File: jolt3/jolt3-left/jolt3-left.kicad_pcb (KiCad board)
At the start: 2 copper layers, 151 x 98 mm, 33 parts, among them J1 Conn_01x02_Pin, J10 Conn_01x02_Pin, J11 Conn_01x02_Pin, J12 Conn_01x02_Pin, J13 Conn_01x02_Pin, J14 Conn_01x02_Pin, J15 Conn_01x02_Pin, J16 Conn_01x02_Pin, J17 Conn_01x02_Pin, J18 Conn_01x02_Pin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

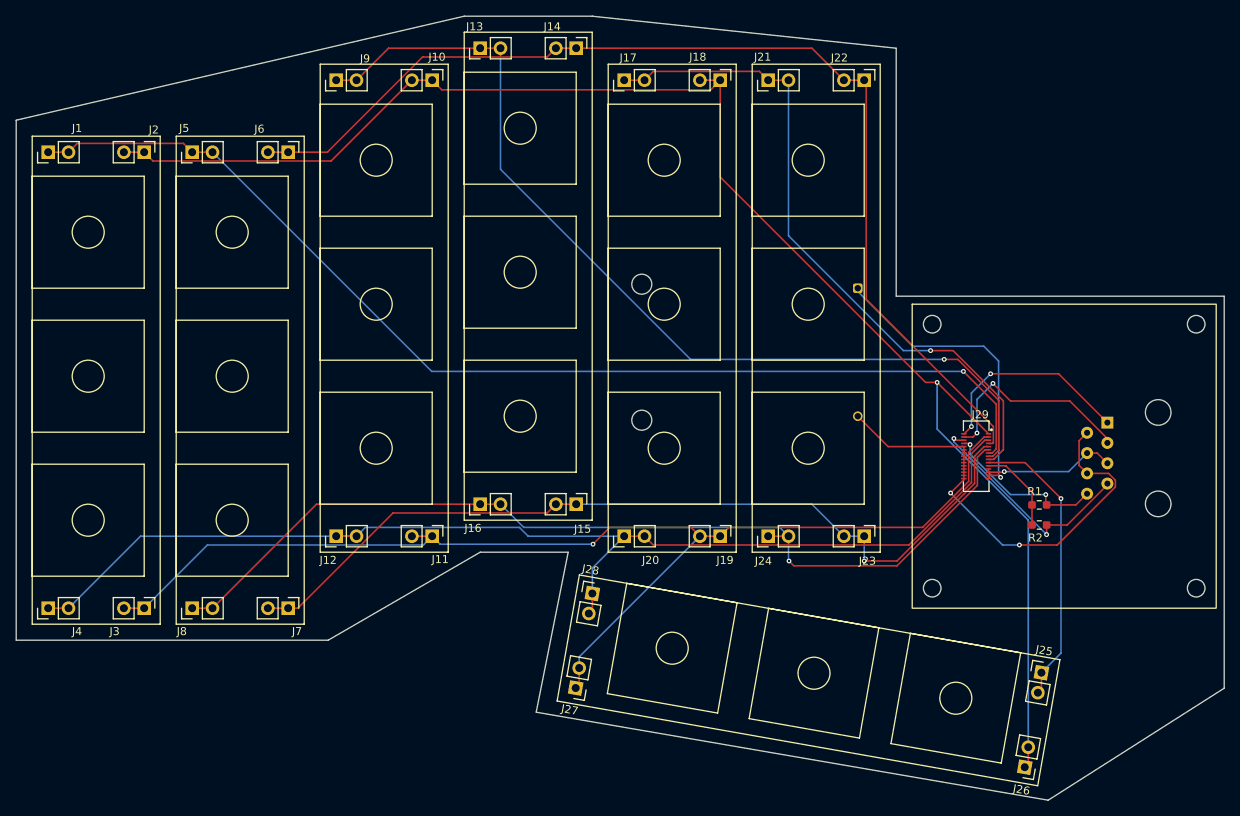
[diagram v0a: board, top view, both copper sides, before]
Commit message: Jolt 3: Rev A for 3 boards
Send Rev A out for jolt3-left, jolt3-right, and j3-mez-2040.
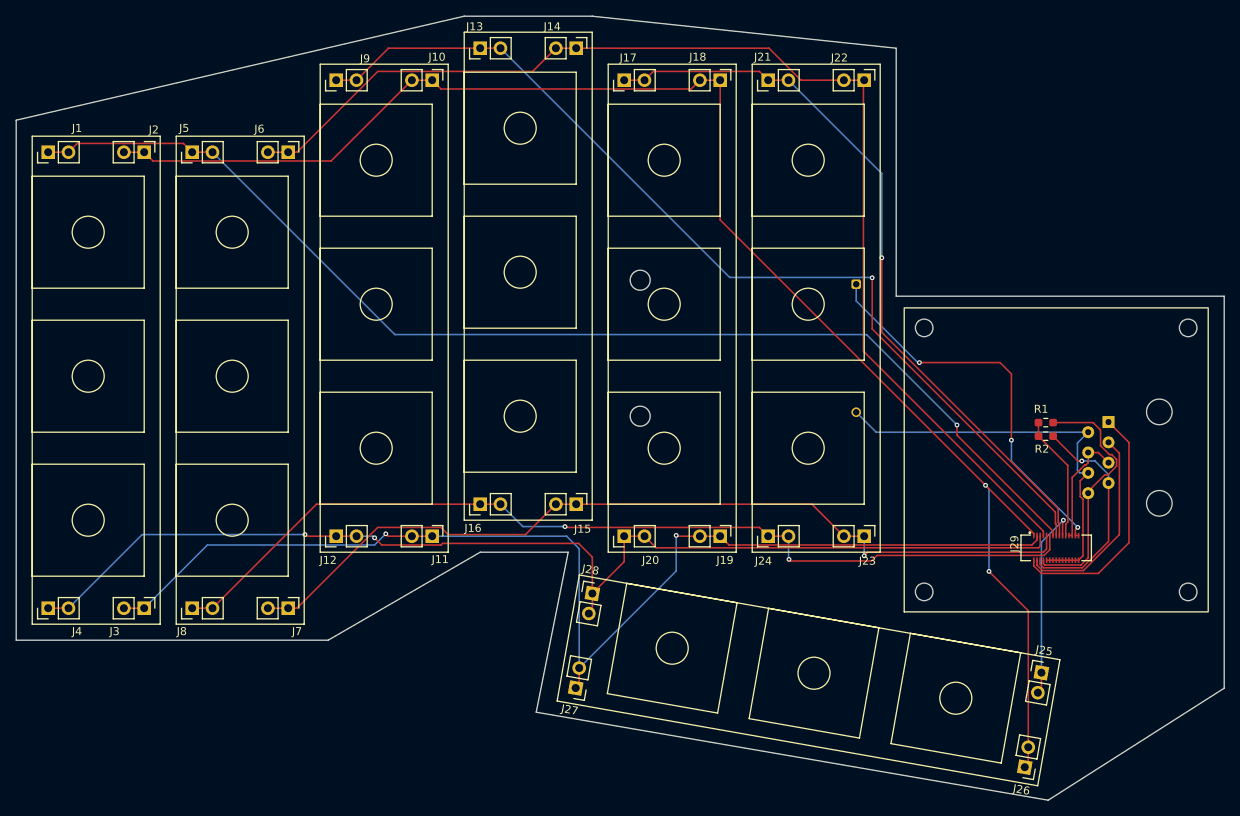
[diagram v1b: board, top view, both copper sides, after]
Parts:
- moved J29 15.2 mm to (167.0, 134.5), turned to 90 degrees
- moved R2 11.1 mm to (165.7, 120.5)
- moved R1 10.3 mm to (165.7, 118.8)
- moved BT1 0.54 mm to (144.0, 125.5)
- moved J31 0.16 mm to (173.5, 118.7)
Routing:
- net /ROW-D: track 134.2 -> 147.9 mm
- net /COL-D: track 36.4 -> 24.8 mm
- net Net-(BT1-+): track 38.5 -> 49.4 mm, vias 1 -> 3
- net /SDA: track 20.6 -> 31.4 mm, vias 2 -> 0
- net /COL-A: track 139.2 -> 147.4 mm
- net /COL-C: track 84.8 -> 92.4 mm
- net GND: track 58.3 -> 52.6 mm, vias 2 -> 0
- net +3.3V: track 10.9 -> 15.7 mm
- net /SER-RX: track 26.0 -> 30.7 mm, vias 2 -> 0
- net /ROW-A: track 194.6 -> 190.9 mm, vias 1 -> 2
- net /COL-B: track 119.4 -> 122.3 mm
- net VBUS: track 16.8 -> 14.8 mm, vias 1 -> 0
- net /ROW-B: track 148.8 -> 147.1 mm, vias 1 -> 2
- net /ROW-E: track 108.1 -> 109.6 mm
- net /SER-TX: track 26.6 -> 25.1 mm, vias 2 -> 0
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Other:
- board text added: "Jolt 3 - Left REV A"
- board text removed: "Jolt 2 - Left REV B"

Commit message: Update for latest KiCad
This seems to have done a rewrite of uuids within the files.
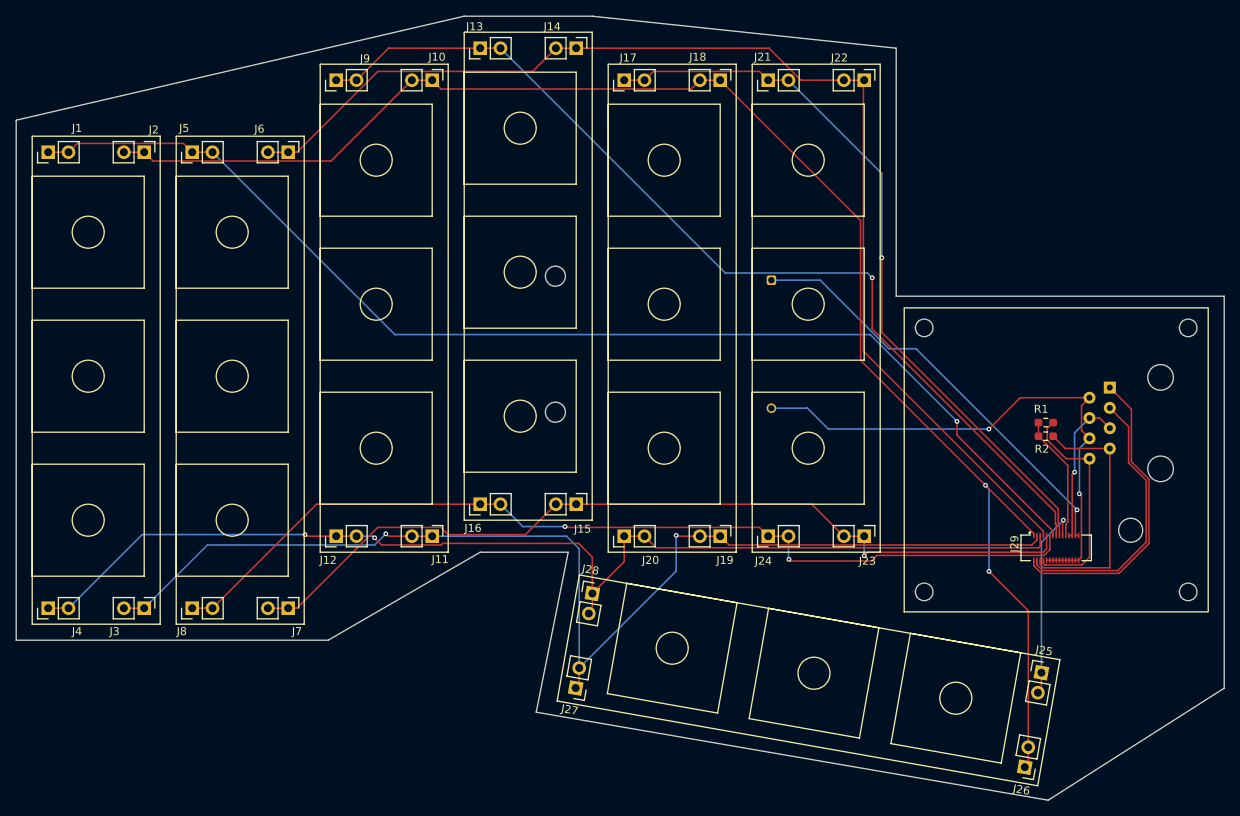
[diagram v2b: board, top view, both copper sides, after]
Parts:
- moved BT1 10.6 mm to (133.4, 125.0)
- moved J31 4.31 mm to (173.7, 114.4)
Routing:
- net GND: track 52.6 -> 68.4 mm, vias 0 -> 2
- net /SER-TX: track 25.1 -> 34.7 mm
- net /SER-RX: track 30.7 -> 38.6 mm
- net Net-(BT1-+): track 49.4 -> 53.8 mm, vias 3 -> 1
- net VBUS: track 14.8 -> 19.1 mm, vias 0 -> 1
- net /SCL: track 27.9 -> 32.0 mm, vias 1 -> 0
- net /SDA: track 31.4 -> 27.7 mm
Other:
- board text added: "Jolt 3 - Left REV B"
- board text removed: "Jolt 3 - Left REV A"
